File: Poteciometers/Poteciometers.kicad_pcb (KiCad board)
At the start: 2 copper layers, 59.5 x 16.3 mm, 16 parts, among them J1 POT_PMOD, J2 EXT_PMOD

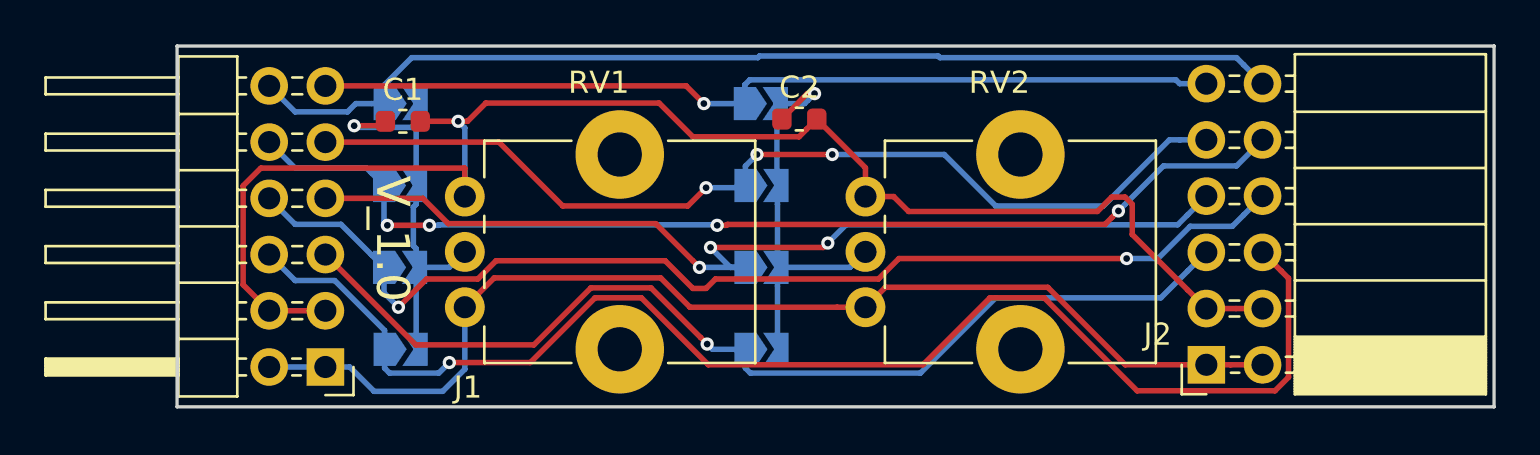
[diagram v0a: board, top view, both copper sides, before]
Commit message: Adding shift by one suggested by tnt
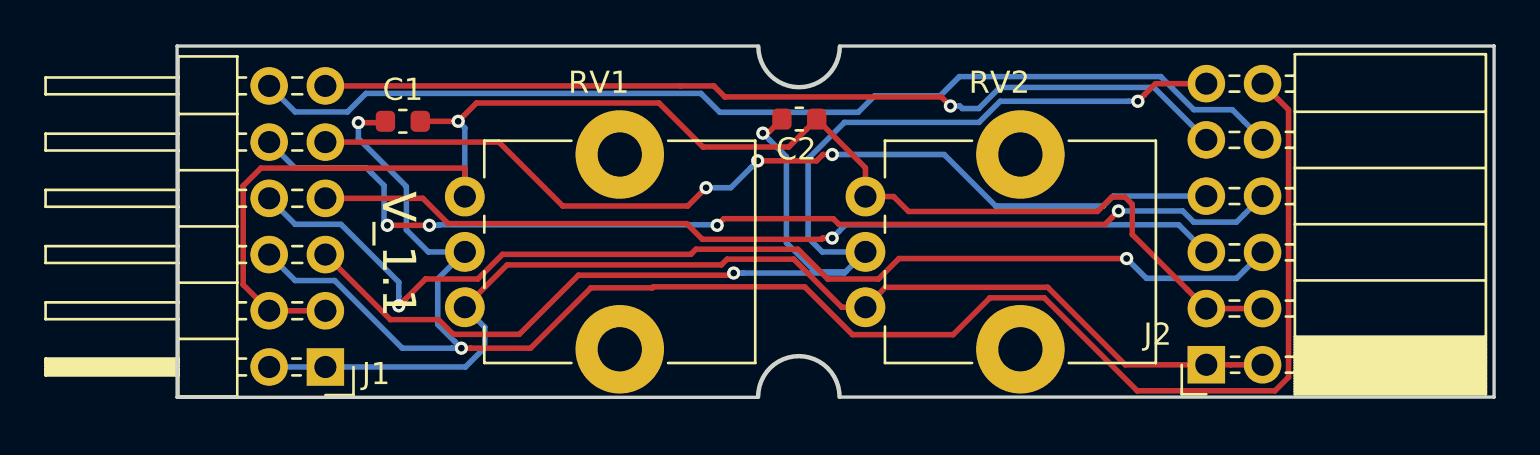
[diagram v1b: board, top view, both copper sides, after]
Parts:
- removed G***: LOGO, parts:OSH_7x7
- removed G***: LOGO, parts:radiona-10mm
- removed JP1: GP14, Jumper:SolderJumper-2_P1.3mm_Open_TrianglePad1.0x1.5mm
- removed JP2: GP15, Jumper:SolderJumper-2_P1.3mm_Open_TrianglePad1.0x1.5mm
- removed JP3: GP16, Jumper:SolderJumper-2_P1.3mm_Open_TrianglePad1.0x1.5mm
- removed JP4: GP17, Jumper:SolderJumper-2_P1.3mm_Open_TrianglePad1.0x1.5mm
- removed JP5: GN14, Jumper:SolderJumper-2_P1.3mm_Open_TrianglePad1.0x1.5mm
- removed JP6: GN15, Jumper:SolderJumper-2_P1.3mm_Open_TrianglePad1.0x1.5mm
- removed JP7: GN16, Jumper:SolderJumper-2_P1.3mm_Open_TrianglePad1.0x1.5mm
- removed JP8: GN17, Jumper:SolderJumper-2_P1.3mm_Open_TrianglePad1.0x1.5mm
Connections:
- C1 pad 1: POT1 -> GP14
- C2 pad 1: POT2 -> GN14
- J2 pad 10: GP16 -> GP17
- J2 pad 11: GN17 -> GN14
- J2 pad 12: GP17 -> GP14
- J2 pad 5: GN14 -> GN15
- J2 pad 6: GP14 -> GP15
- J2 pad 7: GN15 -> GN16
- J2 pad 8: GP15 -> GP16
- J2 pad 9: GN16 -> GN17
- RV1 pad 2: POT1 -> GP14
- RV2 pad 2: POT2 -> GN14
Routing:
- net GP14: track 61.3 -> 81.6 mm, vias 1 -> 2
- net POT2: track 19.2 -> 0.00 mm, vias 1 -> 0
- net POT1: track 19.0 -> 0.00 mm, vias 1 -> 0
- net GN14: track 46.9 -> 63.0 mm, vias 1 -> 3
- net GN15: track 45.6 -> 41.4 mm, vias 3 -> 1
- net GN16: track 44.7 -> 43.1 mm
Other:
- board size 59.5 x 16.3 mm -> 59.5 x 15.9 mm
- board text added: "V_1.1"
- board text removed: "V_1.0"

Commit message: Adding ground plane
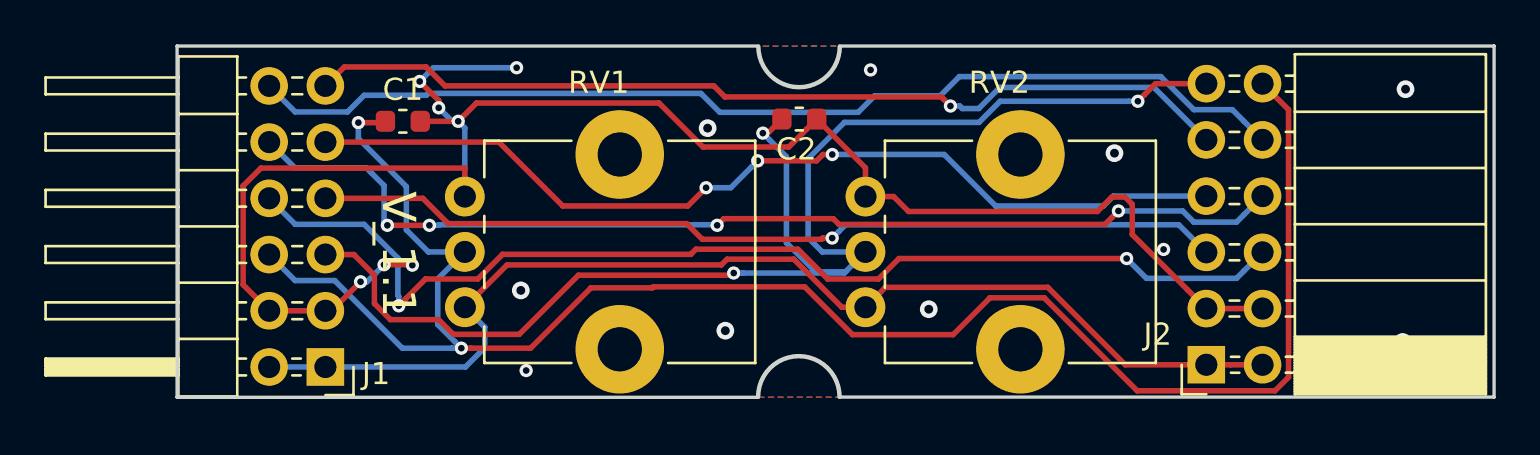
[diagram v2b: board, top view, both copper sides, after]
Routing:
- net GND: track 69.2 -> 81.3 mm, vias 1 -> 17
- net GN14: track 63.0 -> 63.7 mm
- net GN17: track 41.6 -> 42.3 mm
- net GP15: track 50.4 -> 51.0 mm
- added copper zone on B.Cu, net GND
- added copper zone on F.Cu, net GND
